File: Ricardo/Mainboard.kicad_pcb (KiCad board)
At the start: 4 copper layers, 100 x 60 mm, 323 parts, among them J1 USB_B_Micro, J10 Conn_01x02_Male, J11 Conn_01x02_Male, J12 Conn_01x02_Male, J2 8P8C_LED, J3 Micro_SD_Card_Det, J4 Conn_Coaxial, J5 Conn_Coaxial, J6 Screw_Terminal_01x02, J7 Screw_Terminal_01x02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

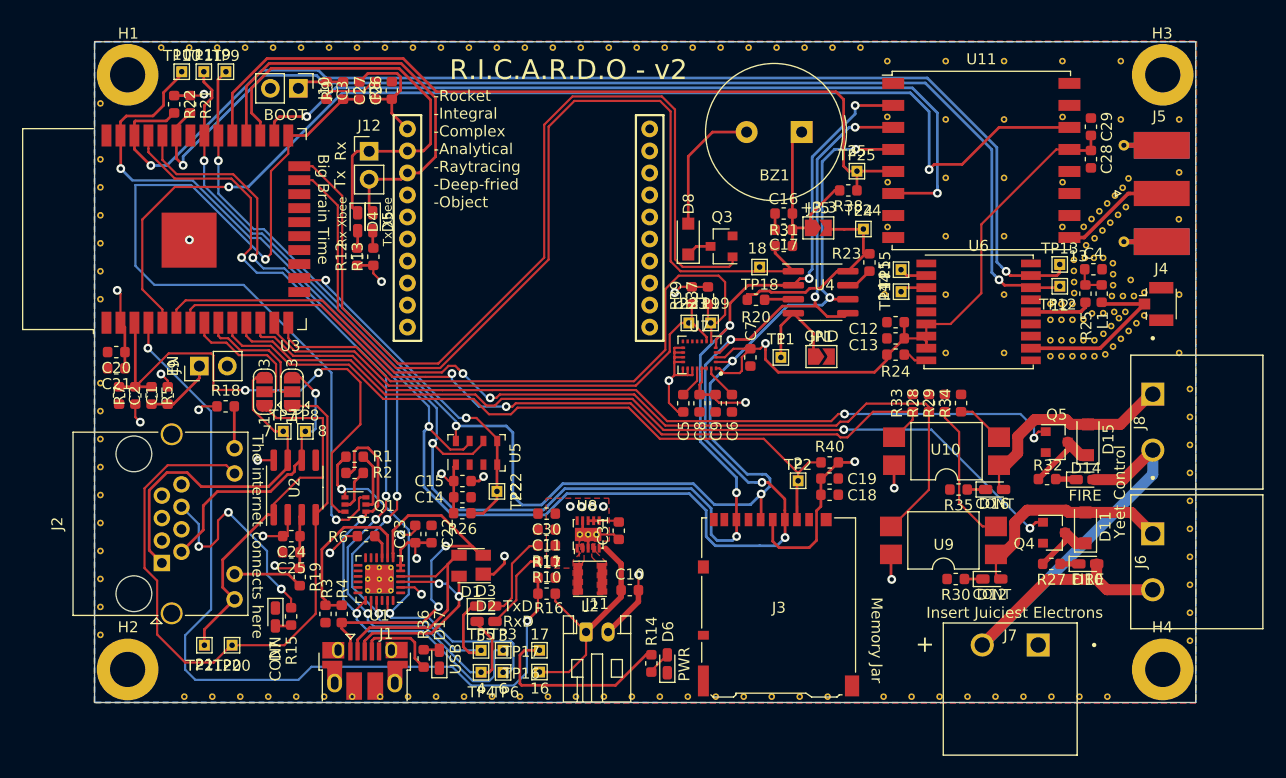
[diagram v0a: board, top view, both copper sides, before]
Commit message: RICARDO-V3 added power through usb, fixed issue with power plane on layer3
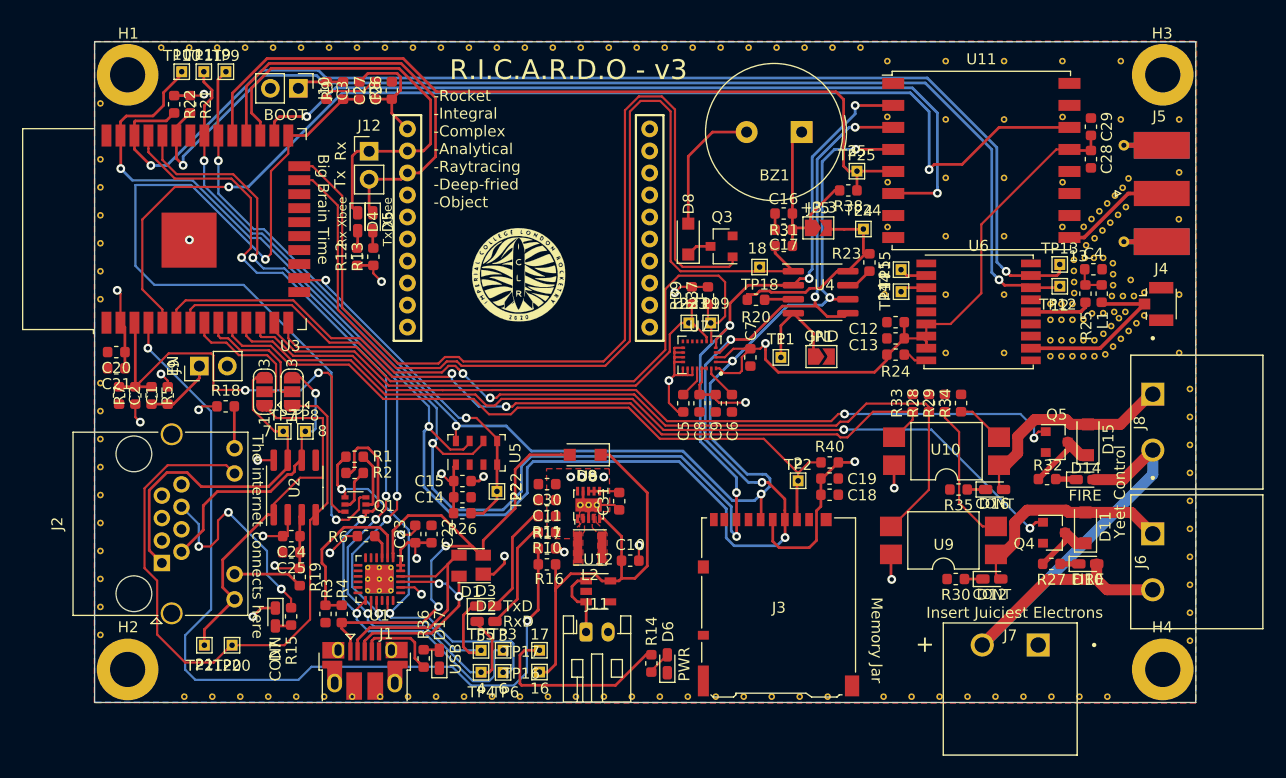
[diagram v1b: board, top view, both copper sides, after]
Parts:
- added D9: D_Schottky, Diode_SMD:D_SOD-123F, F.Cu at (129.6, 87.5)
- added G***: LOGO, iclr-hw:iclr_logo, F.Cu at (123.5, 71.2)
- added U12: MAX40200AUK, Package_TO_SOT_SMD:SOT-23-5, F.Cu at (130.7, 99.9)
- C10, C11, C30: value 10u -> 10uF
- C12, C14, C16, C18, C20, C22, C24, C26, C28: value 100nf -> 100nF
- C13, C15, C17, C19, C21, C23, C25, C27, C29: value 10uf -> 10uF
- C2: value 0.1uF -> 1nF
- C31: value 100n -> 100nF
- R1, R16, R17, R2, R20, R23, R24, R26, R31, R37, R38, R39, R40: value 10k -> 10K
- R27, R30, R32, R35, R6: value 1k -> 1K
- R3: value 22k -> 22K
- R4: value 43k -> 43K
- R8: value 5K -> 10K
- moved L2 2.85 mm to (130.0, 95.9)
- moved C31 2.68 mm to (132.6, 91.7)
- moved U8 2.68 mm to (129.9, 92.1)
- moved C10 2.68 mm to (133.6, 97.1)
- moved C11 2.68 mm to (126.1, 91.6)
- moved C30 2.68 mm to (126.1, 90.2)
- moved R10 2.66 mm to (126.1, 94.5)
- moved R11 2.66 mm to (126.1, 93.1)
- moved R16 2.66 mm to (126.1, 97.5)
- moved R17 2.66 mm to (126.1, 96.0)
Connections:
- J11 pad 1: VDD -> Net-(J11-Pad1)
- J2 pad 3: (no net) -> Net-(J2-Pad3)
- J2 pad 4: (no net) -> Net-(J2-Pad4)
- J2 pad 5: (no net) -> Net-(J2-Pad5)
- J3 pad 1: (no net) -> Net-(J3-Pad1)
- J3 pad 10: (no net) -> Net-(J3-Pad10)
- J3 pad 8: (no net) -> Net-(J3-Pad8)
- J3 pad 9: (no net) -> Net-(J3-Pad9)
- JP2 pad 11: (no net) -> Net-(JP2-Pad11)
- JP2 pad 12: (no net) -> Net-(JP2-Pad12)
- JP2 pad 13: (no net) -> Net-(JP2-Pad13)
- JP2 pad 14: (no net) -> Net-(JP2-Pad14)
- JP2 pad 15: (no net) -> Net-(JP2-Pad15)
- JP2 pad 16: (no net) -> Net-(JP2-Pad16)
- JP2 pad 17: (no net) -> Net-(JP2-Pad17)
- JP2 pad 18: (no net) -> Net-(JP2-Pad18)
- JP2 pad 19: (no net) -> Net-(JP2-Pad19)
- JP2 pad 20: (no net) -> Net-(JP2-Pad20)
- JP2 pad 4: (no net) -> Net-(JP2-Pad4)
- JP2 pad 5: (no net) -> Net-(JP2-Pad5)
- JP2 pad 6: (no net) -> Net-(JP2-Pad6)
- JP2 pad 7: (no net) -> Net-(JP2-Pad7)
- JP2 pad 8: (no net) -> Net-(JP2-Pad8)
- JP2 pad 9: (no net) -> Net-(JP2-Pad9)
- U1 pad 1: (no net) -> Net-(U1-Pad1)
- U1 pad 10: (no net) -> Net-(U1-Pad10)
- U1 pad 11: (no net) -> Net-(U1-Pad11)
- U1 pad 12: (no net) -> Net-(U1-Pad12)
- U1 pad 13: (no net) -> Net-(U1-Pad13)
- U1 pad 14: (no net) -> Net-(U1-Pad14)
- U1 pad 15: (no net) -> Net-(U1-Pad15)
- U1 pad 16: (no net) -> Net-(U1-Pad16)
- U1 pad 17: (no net) -> Net-(U1-Pad17)
- U1 pad 18: (no net) -> Net-(U1-Pad18)
- U1 pad 22: (no net) -> Net-(U1-Pad22)
- U1 pad 24: (no net) -> Net-(U1-Pad24)
- U11 pad 11: (no net) -> Net-(U11-Pad11)
- U11 pad 12: (no net) -> Net-(U11-Pad12)
- U11 pad 15: (no net) -> Net-(U11-Pad15)
- U11 pad 16: (no net) -> Net-(U11-Pad16)
- U11 pad 7: (no net) -> Net-(U11-Pad7)
- U2 pad 5: (no net) -> Net-(U2-Pad5)
- U3 pad 17: (no net) -> Net-(U3-Pad17)
- U3 pad 18: (no net) -> Net-(U3-Pad18)
- U3 pad 19: (no net) -> Net-(U3-Pad19)
- U3 pad 20: (no net) -> Net-(U3-Pad20)
- U3 pad 21: (no net) -> Net-(U3-Pad21)
- U3 pad 22: (no net) -> Net-(U3-Pad22)
- U3 pad 32: (no net) -> Net-(U3-Pad32)
- U6 pad 13: (no net) -> Net-(U6-Pad13)
- U6 pad 15: (no net) -> Net-(U6-Pad15)
- U6 pad 18: (no net) -> Net-(U6-Pad18)
- U6 pad 4: (no net) -> Net-(U6-Pad4)
- U6 pad 5: (no net) -> Net-(U6-Pad5)
- U7 pad 10: (no net) -> Net-(U7-Pad10)
- U7 pad 11: (no net) -> Net-(U7-Pad11)
- U7 pad 12: (no net) -> Net-(U7-Pad12)
- U7 pad 13: (no net) -> Net-(U7-Pad13)
- U7 pad 9: (no net) -> Net-(U7-Pad9)
- U8 pad 11: GND -> (no net)
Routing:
- net VDD: track 22.2 -> 39.5 mm
- net Net-(D1-Pad2): track 34.9 -> 49.4 mm
- net Net-(J11-Pad1): track 0.00 -> 7.17 mm
- net /FLASH_CS: track 92.7 -> 98.2 mm
- net /Buzzer: track 84.9 -> 90.4 mm
- net /SCLK: track 132.3 -> 127.1 mm
- net /MOSI: track 159.8 -> 163.7 mm
- net /EN: track 48.6 -> 45.0 mm
- net /MISO: track 141.7 -> 145.1 mm
- net Net-(R16-Pad2): track 77.0 -> 79.7 mm
- net Net-(D2-Pad2): track 7.44 -> 9.99 mm
- net Net-(D3-Pad2): track 8.03 -> 10.1 mm
- net GND: track 48.0 -> 46.4 mm, vias 10 -> 12
- removed copper zone on In2.Cu, net +3V3
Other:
- board text added: "R.I.C.A.R.D.O - v3"
- board text removed: "R.I.C.A.R.D.O - v2"
